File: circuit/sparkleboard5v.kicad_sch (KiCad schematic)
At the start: 33 parts, among them J3 Conn_01x04_Pin, J4 Conn_01x02_Pin, J5 Conn_01x02_Pin, U6 AP63205WU

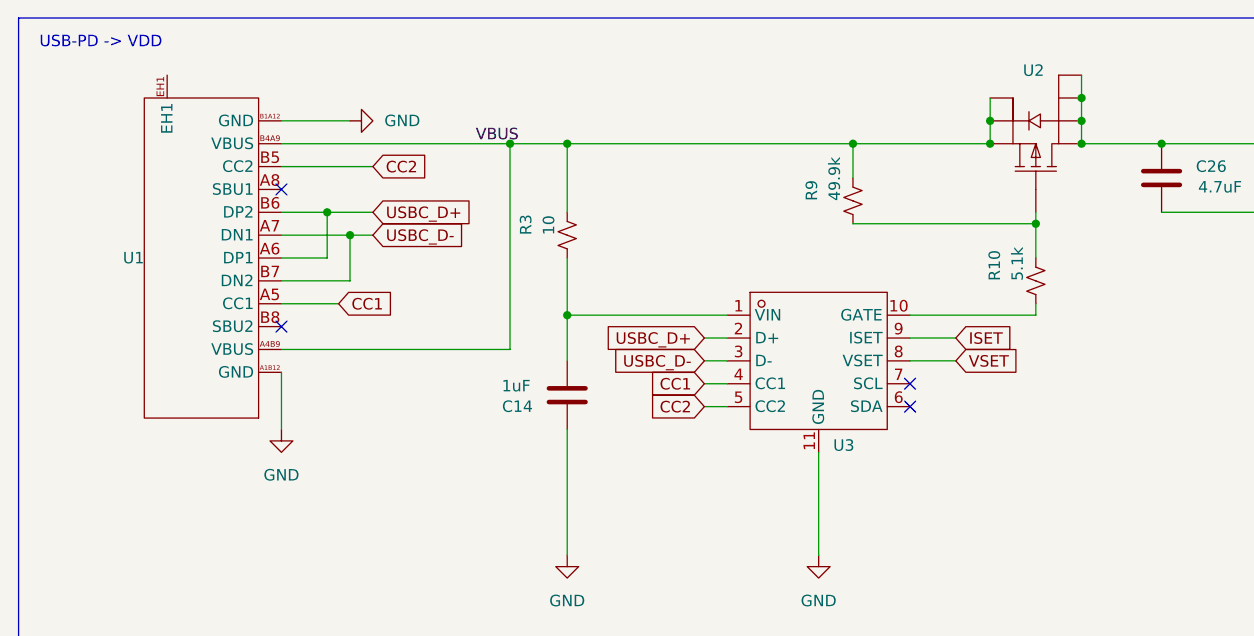
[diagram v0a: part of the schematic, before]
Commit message: tweaked spacing, updated readme
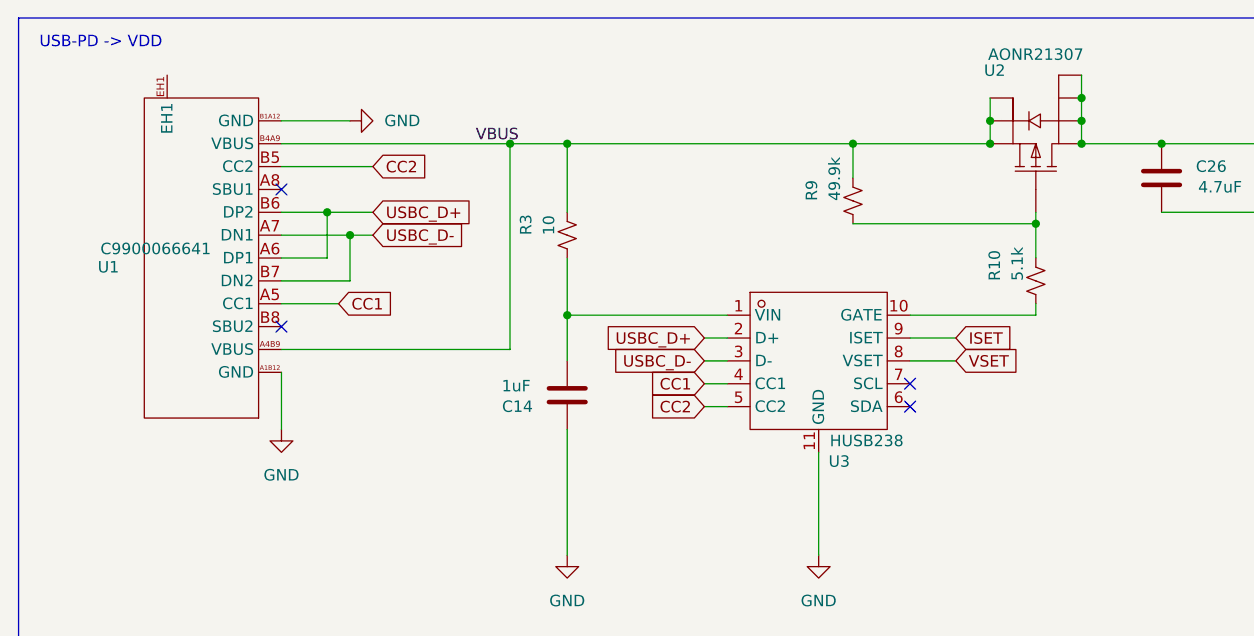
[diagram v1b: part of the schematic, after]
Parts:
- U1: value (none) -> C9900066641
- U2: value (none) -> AONR21307
- U3: value (none) -> HUSB238
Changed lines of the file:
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@@
 		(dnp no)
 		(property "Reference" "U2"
-			(at 128.016 23.622 90)
+			(at 123.698 23.622 90)
 			(show_name no)
 			(do_not_autoplace no)
@@
 			)
 		)
-		(property "Value" ""
-			(at 128.27 31.75 0)
+		(property "Value" "AONR21307"
+			(at 128.27 21.844 90)
 			(show_name no)
 			(do_not_autoplace no)
@@
 		(in_pos_files yes)
 		(dnp no)
-		(fields_autoplaced yes)
 		(property "Reference" "U1"
-			(at 29.21 44.4499 0)
+			(at 26.416 45.466 0)
 			(show_name no)
 			(do_not_autoplace no)
@@
 			)
 		)
-		(property "Value" ""
-			(at 36.83 44.45 0)
+		(property "Value" "C9900066641"
+			(at 30.48 43.434 0)
 			(show_name no)
 			(do_not_autoplace no)
@@
 		(dnp no)
 		(property "Reference" "U3"
-			(at 106.934 65.278 0)
+			(at 106.426 67.056 0)
 			(show_name no)
 			(do_not_autoplace no)
@@
 			)
 		)
-		(property "Value" ""
-			(at 104.14 55.88 0)
+		(property "Value" "HUSB238"
+			(at 109.474 64.77 0)
 			(show_name no)
 			(do_not_autoplace no)

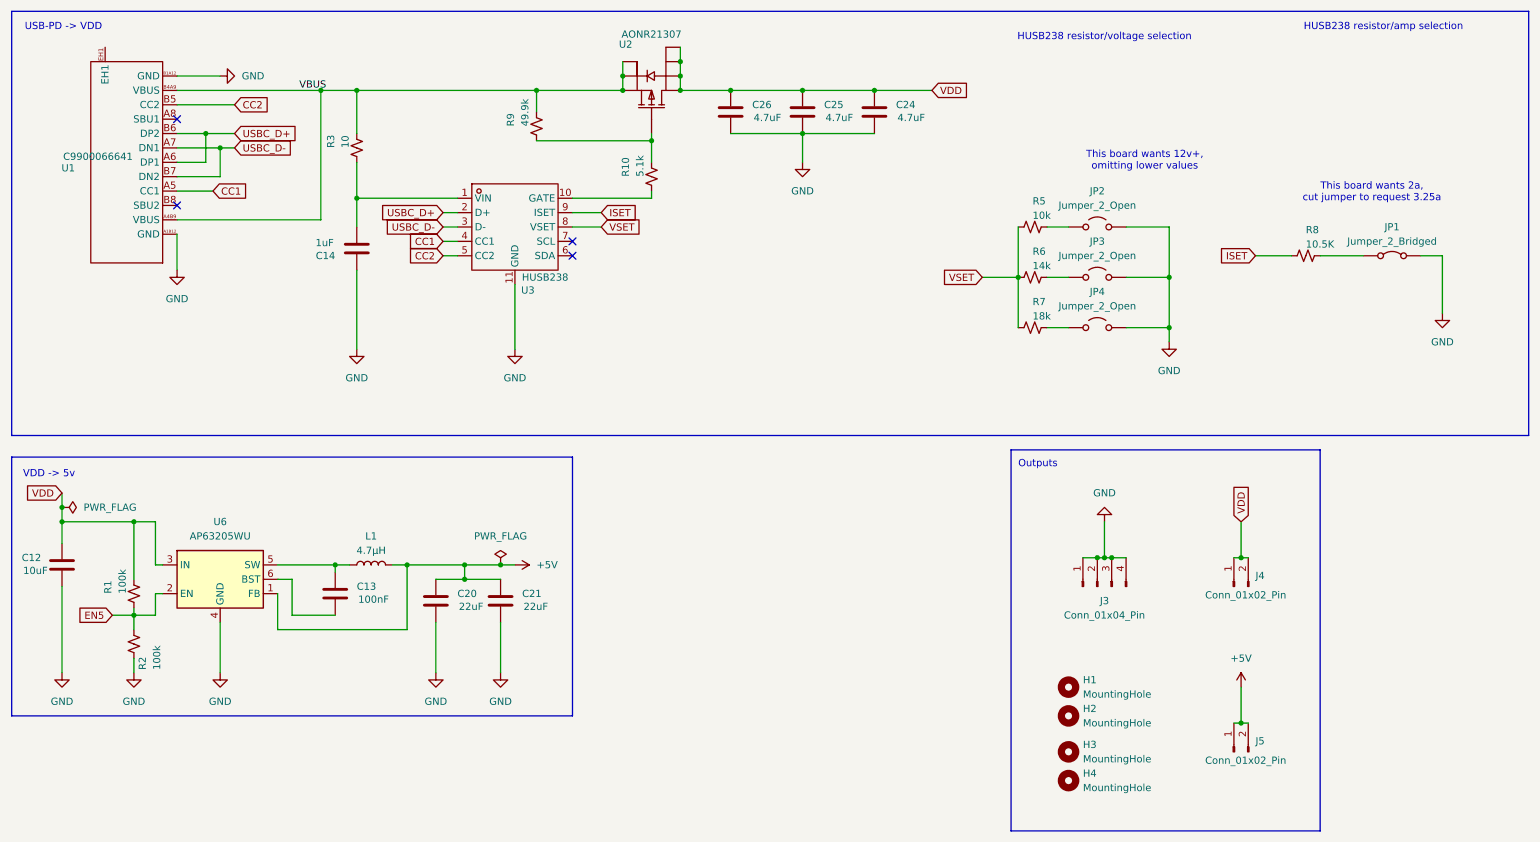
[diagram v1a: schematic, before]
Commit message: Updated board, added more plots for reddit review
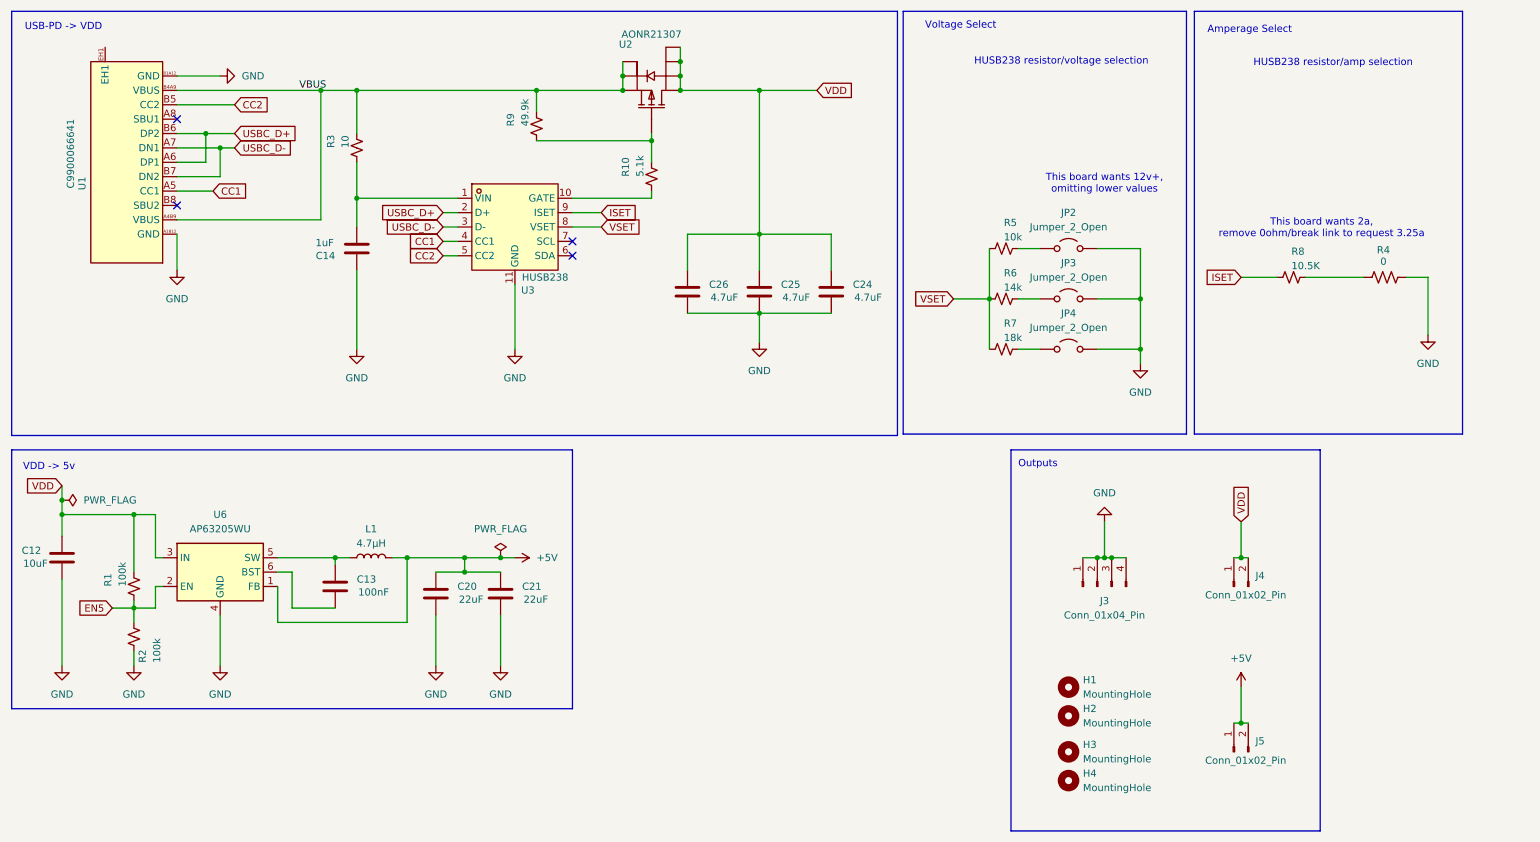
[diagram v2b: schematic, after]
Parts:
- removed JP1: Jumper_2_Bridged, Jumper:SolderJumper-2_P1.3mm_Bridged_Pad1.0x1.5mm, symbol Jumper:Jumper_2_Bridged
- added R4: 0, Resistor_SMD:R_0805_2012Metric, symbol PCM_SparkFun-Resistor:R
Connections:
- net GND: now also R4.1
- net at R8.2: now also R4.2
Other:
- note added: "Amperage Select"
- note added: "This board wants 2a, remove 0ohm/break link to request 3.25a"
- note added: "Voltage Select"
- note removed: "This board wants 2a, cut jumper to request 3.25a"
- moved on the sheet: C12, C13, C20, C21, C24, C25, C26, L1, R1, R2, U6
